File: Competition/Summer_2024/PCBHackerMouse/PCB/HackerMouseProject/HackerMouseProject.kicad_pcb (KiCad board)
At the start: 4 copper layers, 36.4 x 75 mm, 49 parts, among them J1 MicroUSB, J2 UART, J3 Micro_SD, J4 Header4, J5 Header4, J6 POWER, SW1 1825910-6, SW3 1825910-6, U1 ESP32-S3R8, U2 W25Q128JVSIM_TR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

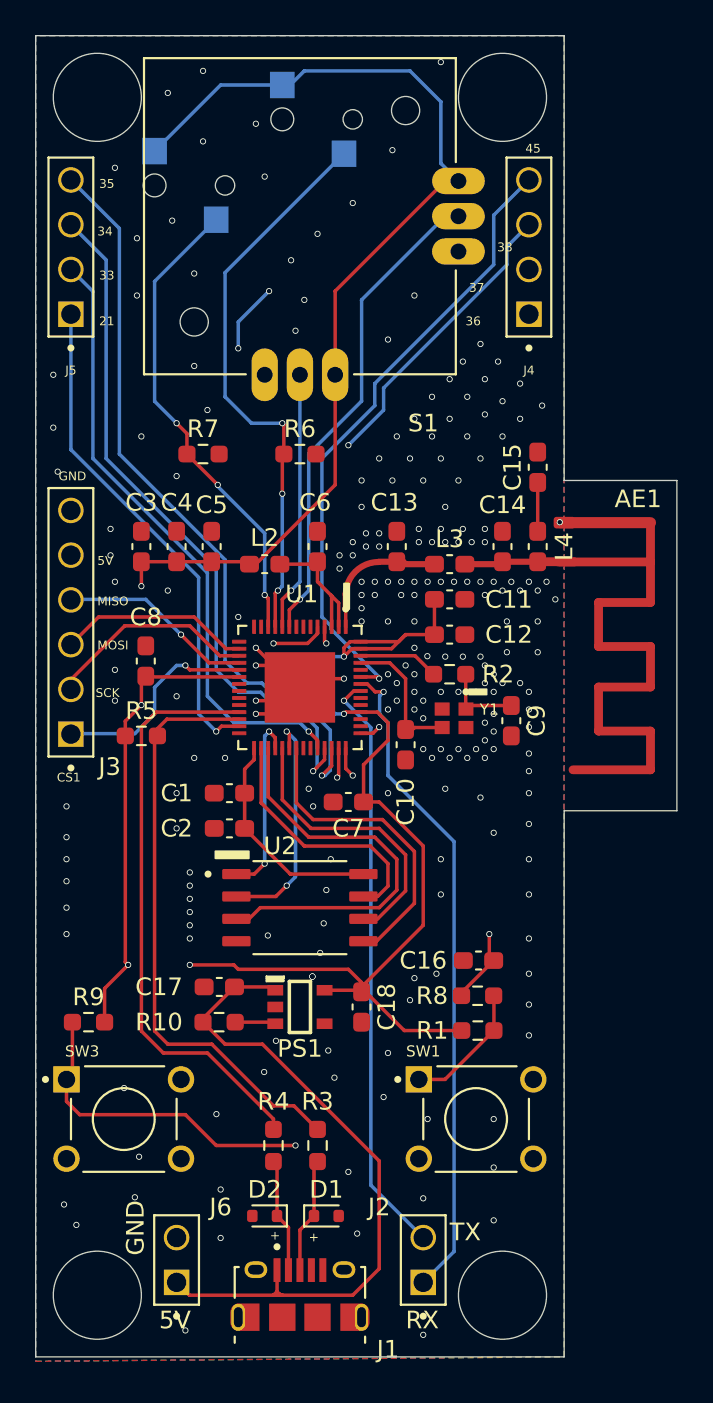
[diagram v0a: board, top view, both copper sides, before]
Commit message: Big vias
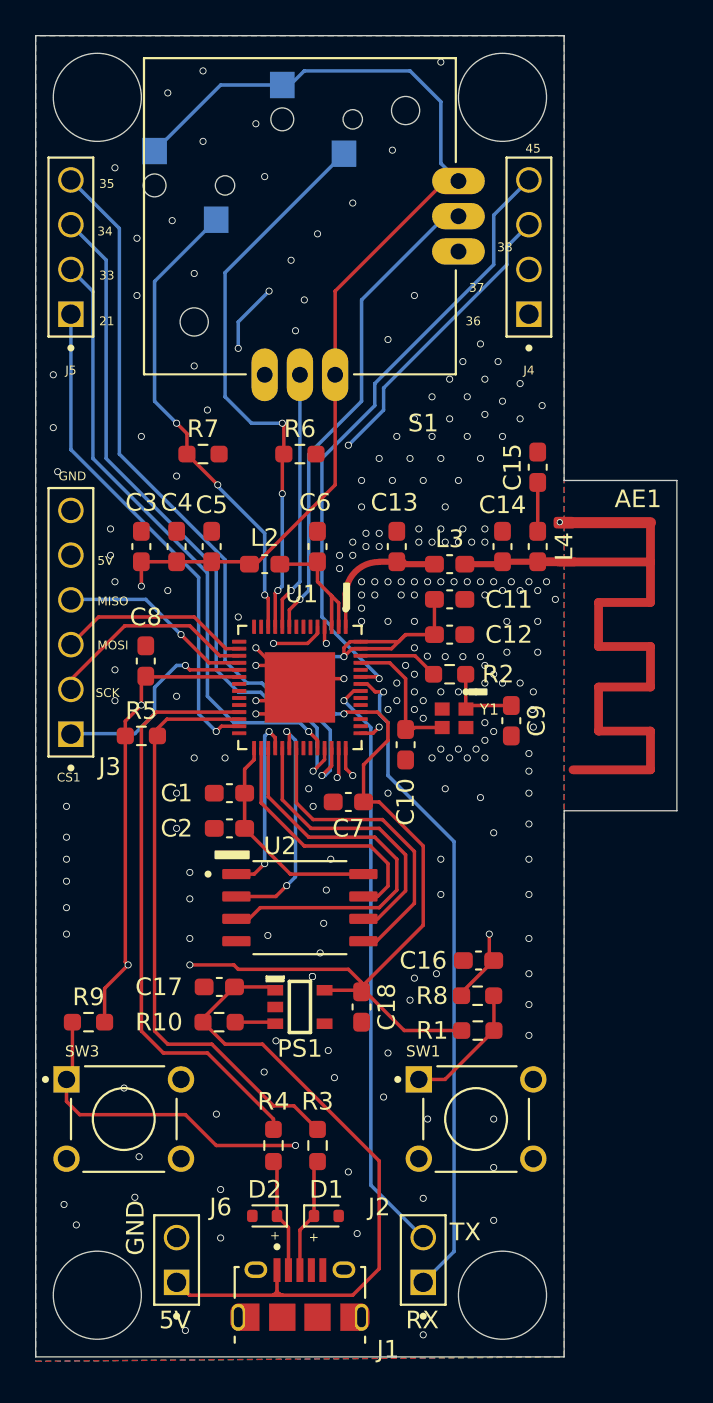
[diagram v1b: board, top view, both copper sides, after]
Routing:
- net GND: vias 224 -> 216

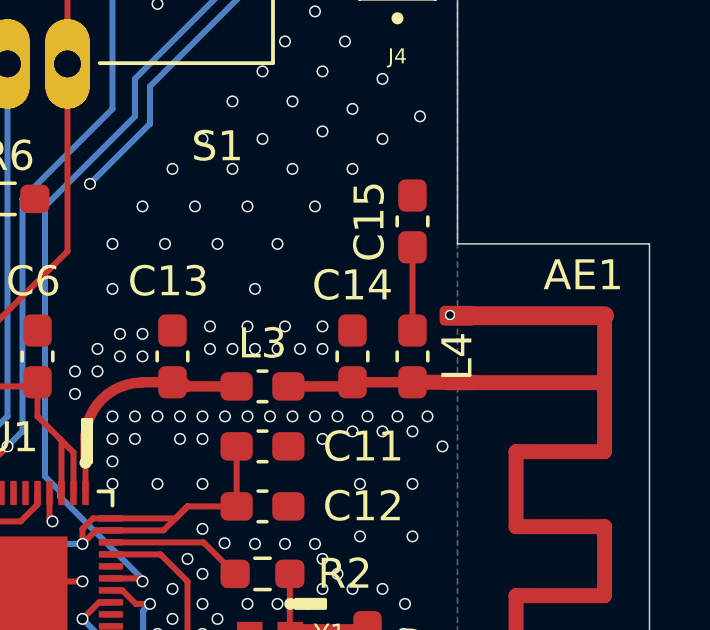
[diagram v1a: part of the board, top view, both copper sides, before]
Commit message: I guess No GND on entenna
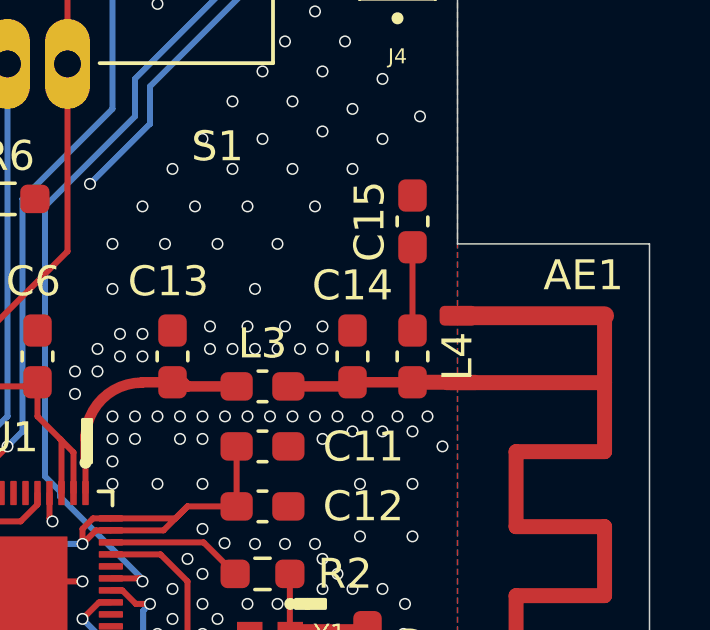
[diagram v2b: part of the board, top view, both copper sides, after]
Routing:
- net GND: vias 216 -> 215
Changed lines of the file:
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@@
-	)
-	(via
-		(at 189.75 61.62)
-		(size 0.35)
-		(drill 0.25)
-		(layers "F.Cu" "B.Cu")
-		(locked yes)
-		(net 1)
 	)
 	(via
